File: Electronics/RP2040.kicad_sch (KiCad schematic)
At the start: 34 parts, among them J1 USB_C_Receptacle_USB2.0, J2 SWD, SW1 SW_Push, U1 W25Q128JVS, U3 RP2040, Y1 12MHz

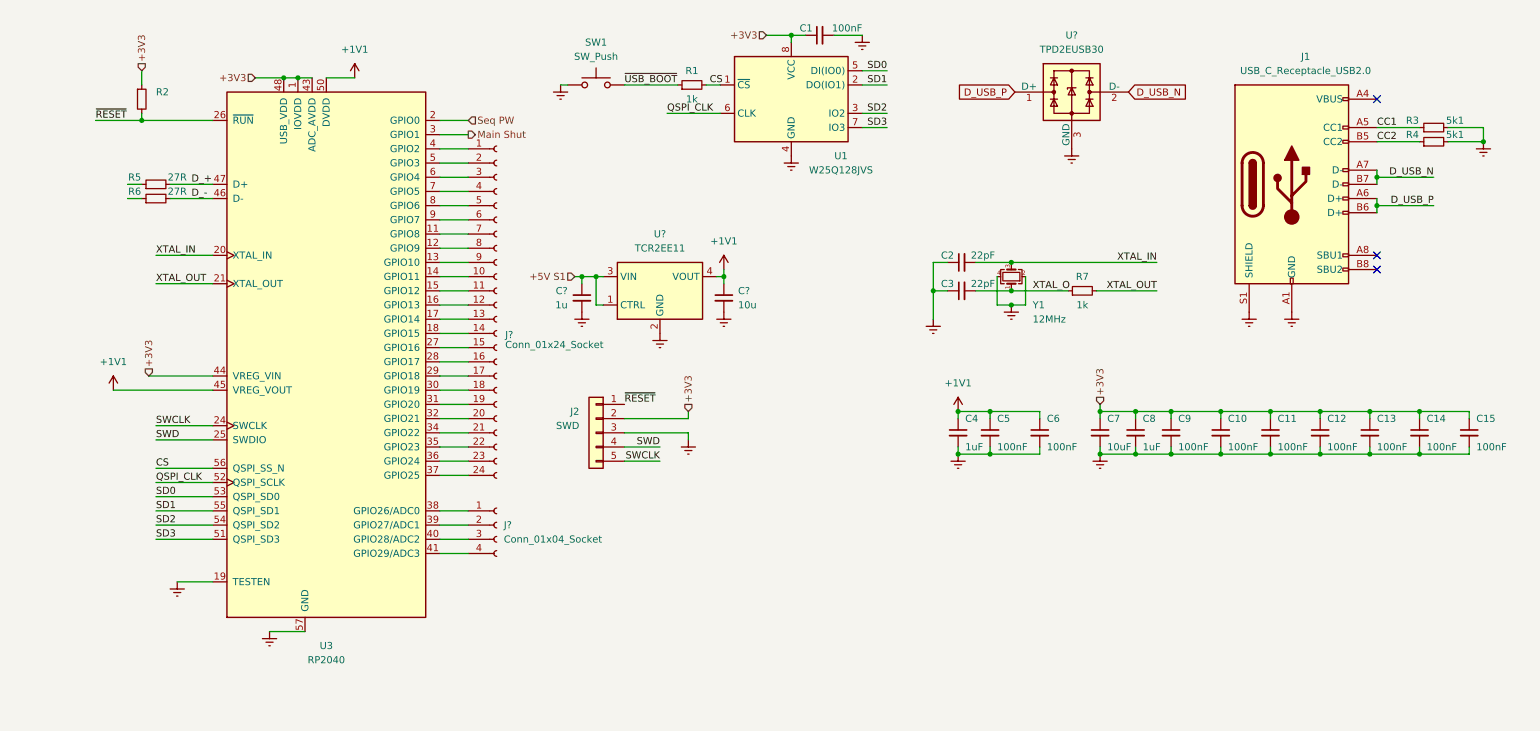
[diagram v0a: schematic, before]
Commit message: Rp2040 Power Sequence finished and general cleaning
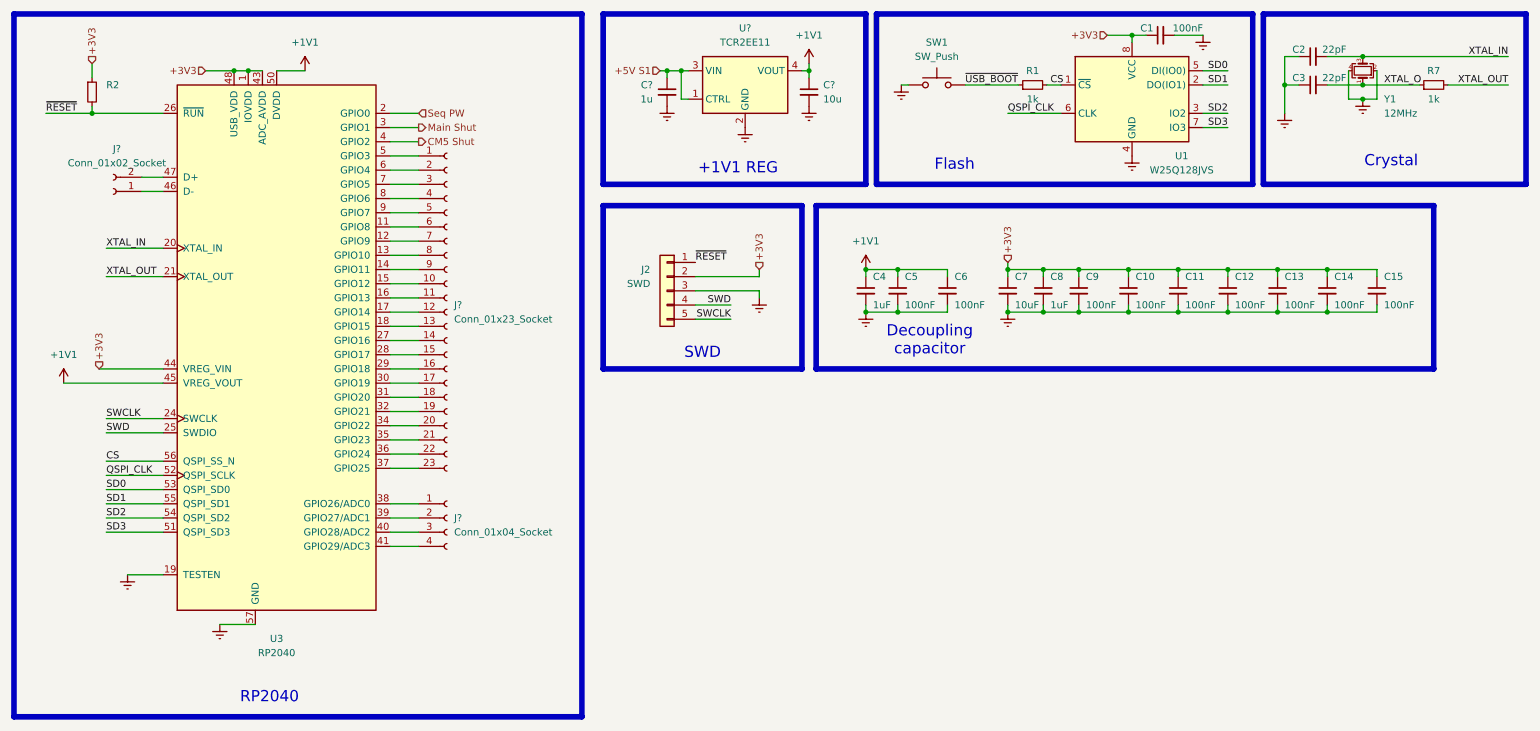
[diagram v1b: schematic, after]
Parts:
- removed J1: USB_C_Receptacle_USB2.0, Connector_USB:USB_C_Receptacle_HRO_TYPE-C-31-M-12, symbol Connector:USB_C_Receptacle_USB2.0
- removed J?: Conn_01x24_Socket, symbol Connector:Conn_01x24_Socket
- removed R3, R4: 5k1, Resistor_SMD:R_0402_1005Metric, symbol Device:R_Small
- removed R5, R6: 27R, Resistor_SMD:R_0603_1608Metric, symbol Device:R_Small
- removed U?: TPD2EUSB30, Package_TO_SOT_SMD:Texas_DRT-3, symbol Power_Protection:TPD2EUSB30
- added J?: Conn_01x02_Socket, symbol Connector:Conn_01x02_Socket
- added J?: Conn_01x23_Socket, symbol Connector:Conn_01x23_Socket
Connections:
- net at U3.11 (GPIO8): now also J?.6 (Pin_6)
- net at U3.12 (GPIO9): now also J?.7 (Pin_7)
- net at U3.13 (GPIO10): now also J?.8 (Pin_8)
- net at U3.14 (GPIO11): now also J?.9 (Pin_9)
- net at U3.15 (GPIO12): now also J?.10 (Pin_10)
- net at U3.16 (GPIO13): now also J?.11 (Pin_11)
- net at U3.17 (GPIO14): now also J?.12 (Pin_12)
- net at U3.18 (GPIO15): now also J?.13 (Pin_13)
- net at U3.27 (GPIO16): now also J?.14 (Pin_14)
- net at U3.28 (GPIO17): now also J?.15 (Pin_15)
- net at U3.29 (GPIO18): now also J?.16 (Pin_16)
- net at U3.30 (GPIO19): now also J?.17 (Pin_17)
- net at U3.31 (GPIO20): now also J?.18 (Pin_18)
- net at U3.32 (GPIO21): now also J?.19 (Pin_19)
- net at U3.34 (GPIO22): now also J?.20 (Pin_20)
- net at U3.35 (GPIO23): now also J?.21 (Pin_21)
- net at U3.36 (GPIO24): now also J?.22 (Pin_22)
- net at U3.37 (GPIO25): now also J?.23 (Pin_23)
- net CM5 Shut: now reaches U3.4 (GPIO2)
- net at U3.5 (GPIO3): now also J?.1 (Pin_1)
- net at U3.6 (GPIO4): now also J?.2 (Pin_2)
- net at U3.7 (GPIO5): now also J?.3 (Pin_3)
- net at U3.8 (GPIO6): now also J?.4 (Pin_4)
- net at U3.9 (GPIO7): now also J?.5 (Pin_5)
- net D_+: no longer names the net of U3.47 (D+)
- net D_+: now also J?.2 (Pin_2)
- net D_-: no longer names the net of U3.46 (D-)
- net D_-: now also J?.1 (Pin_1)
- no-connect marks 3 -> 0
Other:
- moved on the sheet: C1, C10, C11, C12, C13, C14, C15, C2, C3, C4, C5, C6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

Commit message: Footprints Selected
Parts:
- removed J?: Conn_01x02_Socket, symbol Connector:Conn_01x02_Socket
- removed J?: Conn_01x04_Socket, symbol Connector:Conn_01x04_Socket
- removed J?: Conn_01x23_Socket, symbol Connector:Conn_01x23_Socket
- added D24: LED Green, LED_SMD:LED_0603_1608Metric, symbol Device:LED
- added J25: Conn_01x03_Pin, Connector_PinHeader_2.00mm:PinHeader_1x03_P2.00mm_Vertical, symbol Connector:Conn_01x03_Pin
- added J26: Conn_01x03, Connector_JST:JST_GH_SM03B-GHS-TB_1x03-1MP_P1.25mm_Horizontal, symbol Connector:Conn_01x03_Socket
- added R90: 1k, Resistor_SMD:R_0603_1608Metric, symbol Device:R_Small
- added TP11, TP12, TP13, TP14, TP15, TP16, TP17, TP18, TP19, TP20, TP21, TP22, TP23, TP24, TP25, TP26, TP27, TP28, TP29, TP30, TP31, TP32, TP33, TP34, TP35, TP36, TP37, TP38: TestPoint, TestPoint:TestPoint_Pad_1.5x1.5mm, symbol Connector:TestPoint
- C154, C155: renamed from C?; footprint (none) -> Capacitor_SMD:C_0603_1608Metric
- C156: renamed from C4; footprint Capacitor_SMD:C_0402_1005Metric -> Capacitor_SMD:C_0603_1608Metric
- C157: renamed from C5; footprint Capacitor_SMD:C_0402_1005Metric -> Capacitor_SMD:C_0603_1608Metric
- C158: renamed from C6; footprint Capacitor_SMD:C_0402_1005Metric -> Capacitor_SMD:C_0603_1608Metric
- C159: renamed from C7; footprint Capacitor_SMD:C_0402_1005Metric -> Capacitor_SMD:C_0603_1608Metric
- C160: renamed from C8; footprint Capacitor_SMD:C_0402_1005Metric -> Capacitor_SMD:C_0603_1608Metric
- C161: renamed from C9; footprint Capacitor_SMD:C_0402_1005Metric -> Capacitor_SMD:C_0603_1608Metric
- C162: renamed from C10; footprint Capacitor_SMD:C_0402_1005Metric -> Capacitor_SMD:C_0603_1608Metric
- C163: renamed from C1; footprint Capacitor_SMD:C_0402_1005Metric -> Capacitor_SMD:C_0603_1608Metric
- C164: renamed from C11; footprint Capacitor_SMD:C_0402_1005Metric -> Capacitor_SMD:C_0603_1608Metric
- C165: renamed from C12; footprint Capacitor_SMD:C_0402_1005Metric -> Capacitor_SMD:C_0603_1608Metric
- C166: renamed from C13; footprint Capacitor_SMD:C_0402_1005Metric -> Capacitor_SMD:C_0603_1608Metric
- C167: renamed from C2; footprint Capacitor_SMD:C_0402_1005Metric -> Capacitor_SMD:C_0603_1608Metric
- C168: renamed from C3; footprint Capacitor_SMD:C_0402_1005Metric -> Capacitor_SMD:C_0603_1608Metric
- C169: renamed from C14; footprint Capacitor_SMD:C_0402_1005Metric -> Capacitor_SMD:C_0603_1608Metric
- C170: renamed from C15; footprint Capacitor_SMD:C_0402_1005Metric -> Capacitor_SMD:C_0603_1608Metric
- R89: renamed from R2; value ~ -> 10K; footprint (none) -> Resistor_SMD:R_0603_1608Metric
- R91: renamed from R1; footprint Resistor_SMD:R_0402_1005Metric -> Resistor_SMD:R_0603_1608Metric
- R92: renamed from R7; footprint Resistor_SMD:R_0402_1005Metric -> Resistor_SMD:R_0603_1608Metric
- U13: renamed from U3; footprint Sleep-Lib:RP2040-QFN-56 -> Package_DFN_QFN:QFN-56-1EP_7x7mm_P0.4mm_EP3.2x3.2mm
- U15: renamed from U1; footprint Package_SO:SOIC-8_5.23x5.23mm_P1.27mm -> W25Q128JVSIQ TR:SOIC_208MIL_WIN
- Y4: renamed from Y1; footprint Crystal:Crystal_SMD_3225-4Pin_3.2x2.5mm -> ABM3B-12.000MHZ-B2-T:ABM3B
- gave numbers to parts that had none: 1
- renumbered J2 to J27, SW1 to SW2
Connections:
- net IOVDD: now also J26.2 (Pin_2), TP37.1
- net at U13.11 (GPIO8): now also TP15.1
- net at U13.12 (GPIO9): now also TP16.1
- net at U13.13 (GPIO10): now also TP17.1
- net at U13.14 (GPIO11): now also TP18.1
- net at U13.15 (GPIO12): now also TP19.1
- net at U13.16 (GPIO13): now also TP20.1
- net at U13.17 (GPIO14): now also TP21.1
- net at U13.18 (GPIO15): now also TP22.1
- net at U13.27 (GPIO16): now also TP23.1
- net at U13.28 (GPIO17): now also TP24.1
- net at U13.29 (GPIO18): now also TP25.1
- net at U13.30 (GPIO19): now also TP26.1
- net at U13.31 (GPIO20): now also TP27.1
- net at U13.32 (GPIO21): now also TP28.1
- net at U13.34 (GPIO22): now also TP29.1
- net at U13.35 (GPIO23): now also TP30.1
- net at U13.36 (GPIO24): now also TP31.1
- net at U13.37 (GPIO25): now also TP32.1
- net at U13.38 (GPIO26/ADC0): now also TP33.1
- net at U13.39 (GPIO27/ADC1): now also TP34.1
- net at U13.40 (GPIO28/ADC2): now also TP35.1
- net at U13.41 (GPIO29/ADC3): now also TP36.1
- net at U13.46 (D-): now also J25.2 (Pin_2)
- net at U13.47 (D+): now also J25.1 (Pin_1)
- net at U13.5 (GPIO3): now also R90.1
- net at U13.6 (GPIO4): now also TP11.1
- net at U13.7 (GPIO5): now also TP12.1
- net at U13.8 (GPIO6): now also TP13.1
- net at U13.9 (GPIO7): now also TP14.1
- net Seq PW: no longer names the net of U13.2 (GPIO0)
- net Seq PW: now also J26.3 (Pin_3)
- new net: D24.2 (A), R90.2
